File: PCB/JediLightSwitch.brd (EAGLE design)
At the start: 100 x 100 mm, 24 parts, among them U1 APDS-9960, U2 HTU21DSMD, U3 PHOTON_SMD, U4 AT42QT1010SOT23

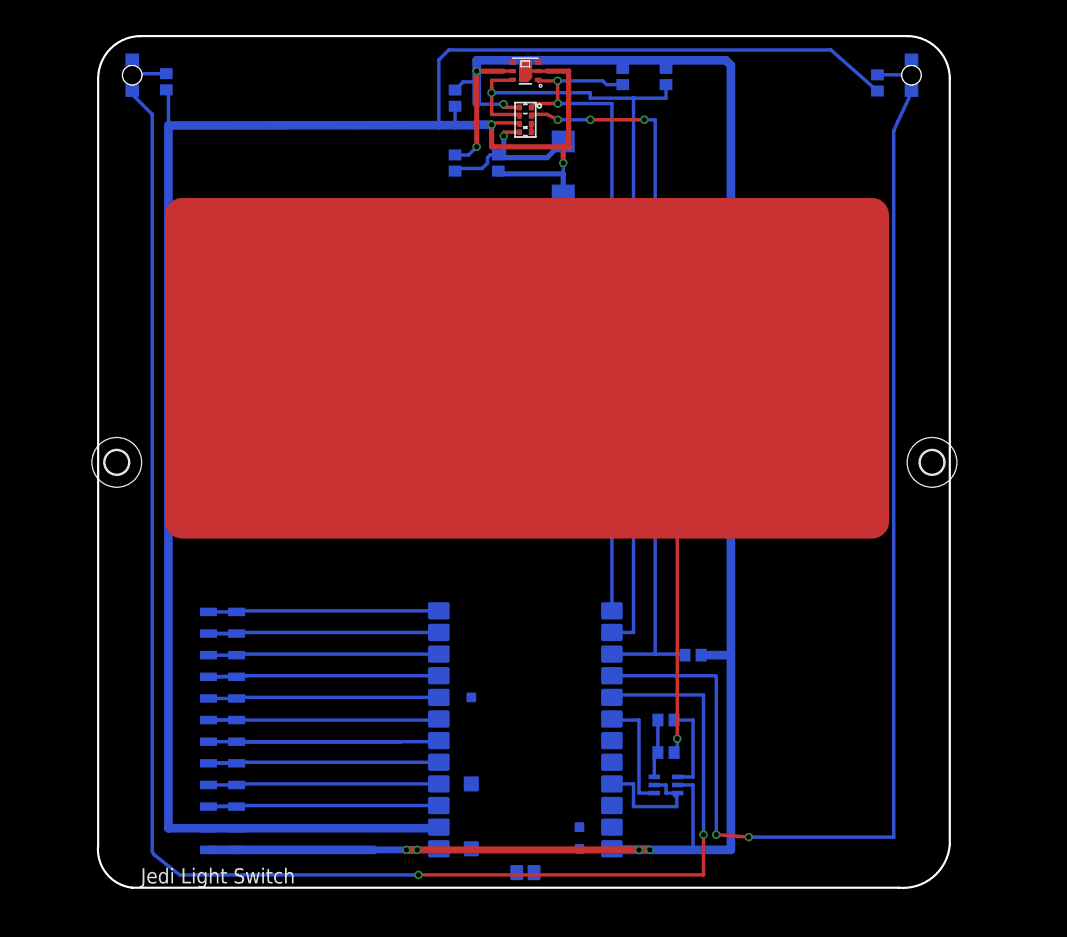
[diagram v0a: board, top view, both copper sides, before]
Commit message: Updated Schematic & PCB: * Added 2x extra LEDs for bottom left/right. * Added second capacitor and resistor options to cap sense circuit. * Cap sense chip is now powered by Photon to allow for re-calibration by power cycle. * Added ground planes for top and bottom of PCB. * Moved some parts in (e.g. resistors for leds and I2C pull-ups) to reduce hit area on enclosure. * Added mode daughter board connectors * Tidied up
Bumped revision of cicuit/board to V1.1
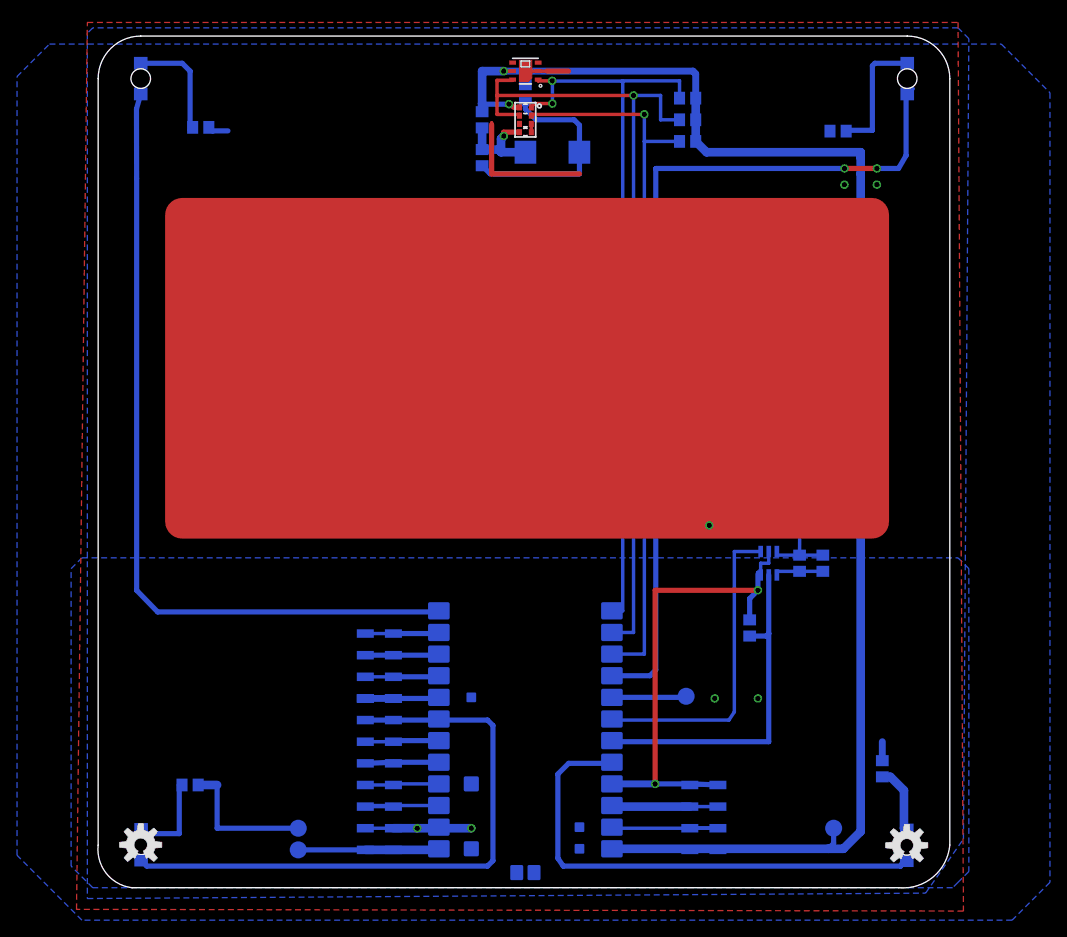
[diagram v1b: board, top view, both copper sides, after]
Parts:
- removed H1, H2: MOUNT-HOLE2.8, holes:2,8
- added C5: DNP, rcl:C0805
- added C6: 0.1uF, rcl:C0805
- added D3, D4: (no value), SparkFun-LED:LED-1206-BOTTOM
- added JP4: (no value), SparkFun-Connectors:1X04_SMD_STRAIGHT_COMBO
- added LOGO1, LOGO2: OSHW-LOGOM, SparkFun-Aesthetics:OSHW-LOGO-M
- added R10: 5k, rcl:R0805
- added R8, R9: 100R, rcl:R0805
- added TP3, TP5, TP6: TPTP20R, testpad:TP20R
- added TP4: 3v3, testpad:TP20R
- JP1, JP2, JP3: value 1X04_SMD_STRAIGHT_COMBO -> (none)
- R7: value 10k -> 5k
- moved R3 60.3 mm to (69.2, 87.6)
- moved JP2 59.2 mm to (71.1, 4.45), turned to 90 degrees
- moved R7 30.4 mm to (81.4, 42.5), turned to 0 degrees
- moved U4 28.7 mm to (78.7, 38.1), turned to 180 degrees
- moved C4 24.2 mm to (82.4, 38.1), turned to 90 degrees
- moved JP1 18.6 mm to (33.0, 29.8)
- moved JP3 18.4 mm to (33.0, 12.1)
- moved C3 8.28 mm to (50.2, 93.3)
- moved R2 8.03 mm to (69.2, 92.7), turned to 180 degrees
- moved R5 7.31 mm to (86.9, 88.8), turned to 0 degrees
- moved R6 6.71 mm to (12.0, 89.3), turned to 180 degrees
- moved R4 5.99 mm to (45.1, 90.2)
- moved R1 5.68 mm to (69.2, 90.2), turned to 180 degrees
- moved C1 2.29 mm to (53.3, 86.4), turned to 0 degrees
- moved C2 2.01 mm to (45.1, 85.7)
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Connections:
- removed net PAD: R7.2, U$1.P$1
- removed net VBAT: U3.22
- removed net VIN: U3.1
- new net 5V: JP3.4, TP3.TP, U3.1
- new net LED3: D3.A, JP4.2, U3.7
- new net LED4: D4.A, U3.20
- new net N$11: JP1.2, U3.10
- new net N$16: JP4.3, U3.6
- new net N$22: TP6.TP, U3.17
- new net N$30: D3.C, R8.1
- new net N$31: D4.C, R9.1
- new net TOUCH_VDD: C6.2, U3.19, U4.5
- net 3.3V: now also JP2.1, TP4.TP; no longer JP3.4, U4.5
- net GND: now also C6.1, JP2.4, R8.2, R9.2, TP5.TP
- net LED1: now also U3.12; no longer U3.17
- net N$10: now also JP4.4, U3.5; no longer JP2.2, U3.7
- net N$12: now also JP1.3, U3.9; no longer JP2.3, U3.6
- net N$13: now also JP1.4, JP4.1, U3.8; no longer JP2.4, U3.5
- net N$19: now also C5.2
- net N$20: now also C5.1
- net N$5: now also JP2.2, U3.23; no longer JP1.1, U3.12
- net N$6: now also JP1.1; no longer JP1.2
- net N$7: now also JP2.3, U3.22; no longer JP1.3, U3.10
- net N$8: now also R10.2, R7.2; no longer JP1.4, U3.9
- net N$9: now also R10.1, U$1.P$1; no longer JP2.1, U3.8
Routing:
- net GND: track 303.1 -> 135.9 mm, vias 2 -> 8
- net LED1: track 188.1 -> 94.9 mm, vias 2 -> 0
- net LED3: track 0.00 -> 73.1 mm
- net PAD: track 61.2 -> 0.00 mm, vias 1 -> 0
- net LED4: track 0.00 -> 59.4 mm
- net 3.3V: track 239.8 -> 187.2 mm, vias 7 -> 2
- net TOUCH_VDD: track 0.00 -> 40.5 mm
- net N$12: track 43.1 -> 5.34 mm
- net LED2: track 140.5 -> 102.9 mm
- net TOUCH: track 13.7 -> 36.9 mm
- net N$8: track 27.1 -> 5.07 mm
- net N$6: track 27.1 -> 5.35 mm
- net N$14: track 24.8 -> 5.37 mm
- net N$10: track 27.1 -> 8.64 mm
- net N$13: track 27.1 -> 8.65 mm
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- added copper zone on layer 1, net GND
- added copper zone on layer 16, net GND
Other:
- board text added: "3v3"
- board text added: "A1"
- board text added: "A2"
- board text added: "A3"
- board text added: "A4"
- board text added: "A5"
- board text added: "DAC"
- board text added: "GND"
- board text added: "Github.com/Tinamous/JediLightSwitch"
- board text added: "Reset"
- board text added: "Rx"
- board text added: "S.Harrison 10-Jan-2016"
- board text added: "Tx"
- board text added: "V1.1"
- board text added: "VBatt"
- board text added: "Vin"
- board text added: "WKP"
- board text removed: "S.Harrison 27-Nov-2015"
- board text removed: "V1"

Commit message: Version 1.2 of Jedi Light Switch as sent to OSH Park.
Added:
* 4x back facing NeoPixes.
* LiPol interface. Charger and monitor.
* 2x IR LEDs
* TEMT6000 light sensor as gesture sensor is very direct


Re-arranged board top so that all the sensors are in a single row.

Moved touch panel up very slightly

Reduced add-on board connectors to 2, one either side of Photon.
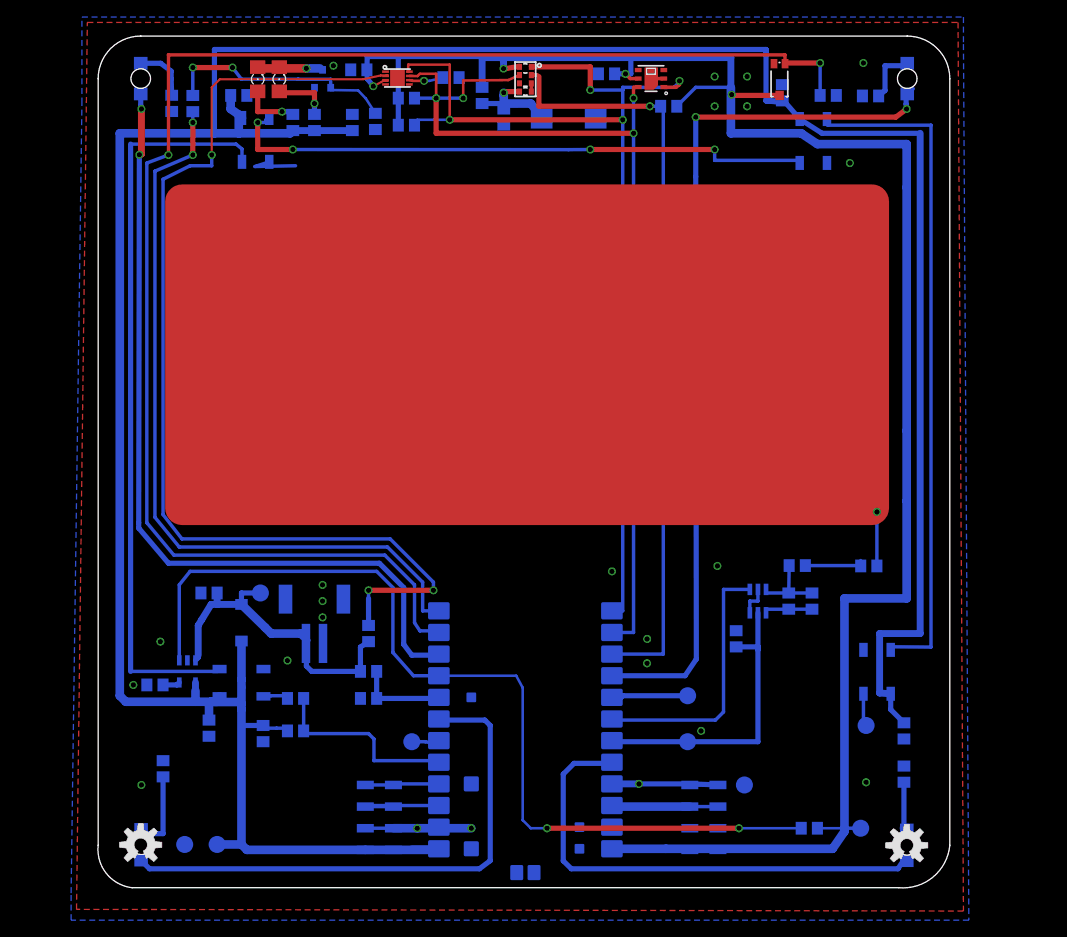
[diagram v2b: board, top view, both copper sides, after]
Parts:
- removed JP1, JP4: (no value), SparkFun-Connectors:1X04_SMD_STRAIGHT_COMBO
- added C10, C7, C8, C9: 0.1uF, rcl:C0805
- added C11, C12: 4.7uF, rcl:C0805
- added C13, C14: 1.0uF, rcl:C0805
- added D5, D6, D7, D8: WS2812B, SparkFun-LED:WS2812B
- added D9: MBRA140, SparkFun-DiscreteSemi:SMA-DIODE
- added FRAME1: FRAME-LETTERNO_PACKAGE, SparkFun-Aesthetics:DUMMY
- added J1: (no value), SparkFun-Connectors:JST-2-SMD
- added LED1, LED2: IR, led:1206
- added Q1: (no value), SparkFun-DiscreteSemi:SOT23-3
- added R11: 470, rcl:R0805
- added R12: DNP, rcl:R0805
- added R13, R14: 100k, rcl:R0805
- added R15, R16, R19: 10k, rcl:R0805
- added R17: 2k, rcl:R0805
- added R18: 10R, rcl:R0805
- added R20, R21: 60R, rcl:R0805
- added R22, R23: 1k, rcl:R0805
- added TP1, TP2, TP7, TP8, TP9: TPTP20R, testpad:TP20R
- added U5: TEMT6000, SparkFun-Sensors:TEMT6000-SEN
- added U6: MCP73831, SparkFun-PowerIC:SOT23-5
- added U7: MAX1704X, SparkFun-PowerIC:TDFN-8
- C4: value 68nF -> 22nF
- R5, R6, R8, R9: value 100R -> 1k
- moved R2 33.2 mm to (36.2, 89.5), turned to 0 degrees
- moved R1 33.1 mm to (36.2, 92.7), turned to 0 degrees
- moved TP6 32.6 mm to (36.8, 17.1)
- moved R10 16.3 mm to (90.5, 37.8), turned to 0 degrees
- moved U2 14.8 mm to (64.9, 95.0)
- moved TP5 13.5 mm to (10.2, 5.08)
- moved C3 9.78 mm to (59.7, 95.6), turned to 0 degrees
- moved TP3 9.55 mm to (14.0, 5.08)
- moved FRAME2 8.35 mm to (19.8, -34.7)
- moved R5 5.62 mm to (90.7, 93.0)
- moved C2 5.40 mm to (47.6, 90.5)
- moved U1 4.76 mm to (50.2, 94.9)
- moved R7 4.72 mm to (82.1, 37.8), turned to 180 degrees
- moved R3 4.69 mm to (67.0, 91.8)
- moved C5 4.62 mm to (83.8, 33.7)
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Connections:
- removed net N$10: JP4.4, U3.5
- new net ALERT: U7.5
- new net BATT_MON: R13.2, R14.1, U3.8
- new net CHARGE_STAT: R16.1, U3.9, U6.1
- new net D4: TP8.TP, U3.17
- new net DAC: TP6.TP, U3.6
- new net IRLED_DRIVE: R18.2, U3.12
- new net LIGHT_LEVEL: R15.1, U3.11, U5.EMITTER
- new net N$17: D5.2, TP1.TP
- new net N$18: D6.4, D7.2
- new net N$21: D5.4, D6.2
- new net N$23: LED2.A, R21.1
- new net N$24: LED1.C, LED2.C, Q1.3
- new net N$25: R22.1, U7.6
- new net NEOPIXELS_DIN: R11.1, R12.2, U3.5
- new net V_BATT: C11.1, D9.A, J1.2, R13.1, R23.1, TP2.TP, U6.3
- net 3.3V: now also C14.1, R16.2, U5.COLLECTOR, U7.3
- net 5V: now also C10.1, C12.2, C13.1, C7.1, C8.1, C9.1, D5.1, D6.1, D7.1, D8.1, D9.C, R12.1, R20.2, R21.2, U6.4
- net GND: now also C10.2, C11.2, C12.1, C13.2, C14.2, C7.2, C8.2, C9.2, D5.3, D6.3, D7.3, D8.3, J1.1, Q1.2, R14.2, R15.2, R17.1, R19.1, R22.2, TP9.TP, U6.2, U7.1, U7.4, U7.EP
- net LED1: now also U3.10; no longer U3.12
- net LED3: no longer JP4.2
- net N$11: now also R17.2, U6.5; no longer JP1.2, U3.10
- net N$12: now also LED1.A, R20.1; no longer JP1.3, U3.9
- net N$13: now also D7.4, D8.2; no longer JP1.4, JP4.1, U3.8
- net N$16: now also R23.2, U7.2; no longer JP4.3, U3.6
- net N$22: now also D8.4, R11.2; no longer TP6.TP, U3.17
- net N$6: now also Q1.1, R18.1, R19.2; no longer JP1.1, U3.11
- net SCL: now also U7.7
- net SDA: now also U7.8
- net TOUCH_VDD: now also TP7.TP
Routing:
- net 5V: track 17.3 -> 361.5 mm
- net LIGHT_LEVEL: track 0.00 -> 180.8 mm, vias 0 -> 2
- net N$16: track 6.37 -> 124.0 mm, vias 0 -> 3
- net CHARGE_STAT: track 0.00 -> 109.1 mm, vias 0 -> 2
- net GND: track 135.9 -> 33.6 mm, vias 8 -> 23
- net IRLED_DRIVE: track 0.00 -> 90.6 mm, vias 0 -> 2
- net N$21: track 0.00 -> 79.2 mm
- net N$13: track 8.65 -> 87.3 mm
- net N$18: track 0.00 -> 70.5 mm, vias 0 -> 4
- net 3.3V: track 187.2 -> 250.9 mm, vias 2 -> 4
- net V_BATT: track 0.00 -> 39.3 mm
- net SDA: track 88.0 -> 123.4 mm, vias 2 -> 4
- net N$9: track 31.3 -> 64.5 mm
- net NEOPIXELS_DIN: track 0.00 -> 22.7 mm
- net N$6: track 5.35 -> 28.0 mm, vias 0 -> 2
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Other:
- board text added: "Dout"
- board text added: "S.Harrison 12-Jan-2016"
- board text added: "V1.2"
- board text removed: "A1"
- board text removed: "A2"
- board text removed: "A3"
- board text removed: "A4"
- board text removed: "A5"
- board text removed: "S.Harrison 10-Jan-2016"
- board text removed: "V1.1"
- board text removed: "WKP"

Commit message: Updated resistor values.
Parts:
- R10, R7: value 5k -> 4k7
- R20, R21: value 60R -> 62R
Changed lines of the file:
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@@
 <attribute name="NAME" x="77.5335" y="36.8935" size="0.8128" layer="26" rot="MR180"/>
 </element>
-<element name="R7" library="rcl" package="R0805" value="5k" x="82.0875" y="37.825" smashed="yes" rot="MR180">
+<element name="R7" library="rcl" package="R0805" value="4k7" x="82.0875" y="37.825" smashed="yes" rot="MR180">
 <attribute name="NAME" x="82.695" y="39.645" size="0.8128" layer="26" rot="MR180"/>
 <attribute name="VALUE" x="79.9725" y="38.7875" size="0.8128" layer="27"/>
@@
 </element>
 <element name="LOGO1" library="SparkFun-Aesthetics" package="OSHW-LOGO-M" value="OSHW-LOGOM" x="94.95" y="4.98" locked="yes"/>
-<element name="R10" library="rcl" package="R0805" value="5k" x="90.4875" y="37.7825" smashed="yes" rot="MR0">
+<element name="R10" library="rcl" package="R0805" value="4k7" x="90.4875" y="37.7825" smashed="yes" rot="MR0">
 <attribute name="NAME" x="92.3925" y="38.735" size="0.8128" layer="26" rot="MR0"/>
 <attribute name="VALUE" x="88.5825" y="38.735" size="0.8128" layer="27"/>
@@
 <element name="LED1" library="led" package="1206" value="IR" x="21.2725" y="94.9325" locked="yes" smashed="yes" rot="R90"/>
 <element name="LED2" library="led" package="1206" value="IR" x="18.7325" y="94.9325" locked="yes" smashed="yes" rot="R90"/>
-<element name="R20" library="rcl" package="R0805" value="60R" x="25.4" y="89.8525" smashed="yes" rot="MR270">
+<element name="R20" library="rcl" package="R0805" value="62R" x="25.4" y="89.8525" smashed="yes" rot="MR270">
 <attribute name="NAME" x="26.67" y="92.075" size="0.8128" layer="26" rot="MR0"/>
 <attribute name="VALUE" x="26.3525" y="86.995" size="0.8128" layer="28" rot="MR0"/>
 </element>
-<element name="R21" library="rcl" package="R0805" value="60R" x="22.86" y="89.8525" smashed="yes" rot="MR270">
+<element name="R21" library="rcl" package="R0805" value="62R" x="22.86" y="89.8525" smashed="yes" rot="MR270">
 <attribute name="NAME" x="23.8125" y="92.075" size="0.8128" layer="26" rot="MR0"/>
 <attribute name="VALUE" x="23.8125" y="86.995" size="0.8128" layer="28" rot="MR0"/>
